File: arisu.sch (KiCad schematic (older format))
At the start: 40 parts, among them J1 USB_B_Micro, J10 PF6, J11 PF7, J12 VCC, J13 D+, J14 D-, J15 GND, J2 MISO, J3 VCC, J4 SCK, J5 MOSI, J6 RES, J7 GND, J8 PF4, J9 PF5, U1 USBLC6-2SC6, U2 ATmega32U4-AU, Y1 Crystal_GND24

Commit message: Initial project update
- Imported FateParts library
- Updated schematic with full backspace switch and stepped capslock switch
- Added new switch footprints to layout
- Updated some traces in layout
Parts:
- U1: symbol Power_Protection:USBLC6-2SC6 -> arisu-rescue:USBLC6-2SC6-Power_Protection
- U2: symbol MCU_Microchip_ATmega:ATmega32U4-AU -> arisu-rescue:ATmega32U4-AU-MCU_Microchip_ATmega
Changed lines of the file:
@@
 EESchema Schematic File Version 4
-LIBS:arisu-cache
-EELAYER 26 0
+EELAYER 30 0
 EELAYER END
 $Descr A4 11693 8268
@@
 $EndDescr
 $Comp
-L MCU_Microchip_ATmega:ATmega32U4-AU U2
+L arisu-rescue:ATmega32U4-AU-MCU_Microchip_ATmega U2
 U 1 1 5C4B1F82
 P 4500 4250
@@
 $EndComp
 $Comp
-L Power_Protection:USBLC6-2SC6 U1
+L arisu-rescue:USBLC6-2SC6-Power_Protection U1
 U 1 1 5C4B2347
 P 1900 5650
@@
 	1    0    0    -1
 $EndComp
+$Comp
+L Mechanical:MountingHole H3
+U 1 1 5C59C18D
+P 8700 3100
+F 0 "H3" H 8800 3146 50  0000 L CNN
+F 1 "MountingHole" H 8800 3055 50  0000 L CNN
+F 2 "Mounting_Holes:MountingHole_2.2mm_M2_Pad" H 8700 3100 50  0001 C CNN
+F 3 "~" H 8700 3100 50  0001 C CNN
+	1    8700 3100
+	1    0    0    -1
+$EndComp
+$Comp
+L Mechanical:MountingHole H4
+U 1 1 5C59C1E9
+P 8700 3300
+F 0 "H4" H 8800 3346 50  0000 L CNN
+F 1 "MountingHole" H 8800 3255 50  0000 L CNN
+F 2 "Mounting_Holes:MountingHole_2.2mm_M2_Pad" H 8700 3300 50  0001 C CNN
+F 3 "~" H 8700 3300 50  0001 C CNN
+	1    8700 3300
+	1    0    0    -1
+$EndComp
+$Comp
+L Mechanical:MountingHole H5
+U 1 1 5C59C249
+P 8700 3500
+F 0 "H5" H 8800 3546 50  0000 L CNN
+F 1 "MountingHole" H 8800 3455 50  0000 L CNN
+F 2 "Mounting_Holes:MountingHole_2.2mm_M2_Pad" H 8700 3500 50  0001 C CNN
+F 3 "~" H 8700 3500 50  0001 C CNN
+	1    8700 3500
+	1    0    0    -1
+$EndComp
+$Comp
+L Mechanical:MountingHole H6
+U 1 1 5C59C2A7
+P 8700 3700
+F 0 "H6" H 8800 3746 50  0000 L CNN
+F 1 "MountingHole" H 8800 3655 50  0000 L CNN
+F 2 "Mounting_Holes:MountingHole_2.2mm_M2_Pad" H 8700 3700 50  0001 C CNN
+F 3 "~" H 8700 3700 50  0001 C CNN
+	1    8700 3700
+	1    0    0    -1
+$EndComp
+$Comp
+L Mechanical:MountingHole H7
+U 1 1 5C59C305
+P 8700 3900
+F 0 "H7" H 8800 3946 50  0000 L CNN
+F 1 "MountingHole" H 8800 3855 50  0000 L CNN
+F 2 "Mounting_Holes:MountingHole_2.2mm_M2_Pad" H 8700 3900 50  0001 C CNN
+F 3 "~" H 8700 3900 50  0001 C CNN
+	1    8700 3900
+	1    0    0    -1
+$EndComp
+$Comp
+L Mechanical:MountingHole H8
+U 1 1 5C59C367
+P 8700 4100
+F 0 "H8" H 8800 4146 50  0000 L CNN
+F 1 "MountingHole" H 8800 4055 50  0000 L CNN
+F 2 "Mounting_Holes:MountingHole_2.2mm_M2_Pad" H 8700 4100 50  0001 C CNN
+F 3 "~" H 8700 4100 50  0001 C CNN
+	1    8700 4100
+	1    0    0    -1
+$EndComp
 Wire Bus Line
 	5750 2700 5750 3150
@@
 Wire Bus Line
 	7050 2650 7050 5800
-$Comp
-L Mechanical:MountingHole H3
-U 1 1 5C59C18D
-P 8700 3100
-F 0 "H3" H 8800 3146 50  0000 L CNN
-F 1 "MountingHole" H 8800 3055 50  0000 L CNN
-F 2 "Mounting_Holes:MountingHole_2.2mm_M2_Pad" H 8700 3100 50  0001 C CNN
-F 3 "~" H 8700 3100 50  0001 C CNN
-	1    8700 3100
-	1    0    0    -1
-$EndComp
-$Comp
-L Mechanical:MountingHole H4
-U 1 1 5C59C1E9
-P 8700 3300
-F 0 "H4" H 8800 3346 50  0000 L CNN
-F 1 "MountingHole" H 8800 3255 50  0000 L CNN
-F 2 "Mounting_Holes:MountingHole_2.2mm_M2_Pad" H 8700 3300 50  0001 C CNN
-F 3 "~" H 8700 3300 50  0001 C CNN
-	1    8700 3300
-	1    0    0    -1
-$EndComp
-$Comp
-L Mechanical:MountingHole H5
-U 1 1 5C59C249
-P 8700 3500
-F 0 "H5" H 8800 3546 50  0000 L CNN
-F 1 "MountingHole" H 8800 3455 50  0000 L CNN
-F 2 "Mounting_Holes:MountingHole_2.2mm_M2_Pad" H 8700 3500 50  0001 C CNN
-F 3 "~" H 8700 3500 50  0001 C CNN
-	1    8700 3500
-	1    0    0    -1
-$EndComp
-$Comp
-L Mechanical:MountingHole H6
-U 1 1 5C59C2A7
-P 8700 3700
-F 0 "H6" H 8800 3746 50  0000 L CNN
-F 1 "MountingHole" H 8800 3655 50  0000 L CNN
-F 2 "Mounting_Holes:MountingHole_2.2mm_M2_Pad" H 8700 3700 50  0001 C CNN
-F 3 "~" H 8700 3700 50  0001 C CNN
-	1    8700 3700
-	1    0    0    -1
-$EndComp
-$Comp
-L Mechanical:MountingHole H7
-U 1 1 5C59C305
-P 8700 3900
-F 0 "H7" H 8800 3946 50  0000 L CNN
-F 1 "MountingHole" H 8800 3855 50  0000 L CNN
-F 2 "Mounting_Holes:MountingHole_2.2mm_M2_Pad" H 8700 3900 50  0001 C CNN
-F 3 "~" H 8700 3900 50  0001 C CNN
-	1    8700 3900
-	1    0    0    -1
-$EndComp
-$Comp
-L Mechanical:MountingHole H8
-U 1 1 5C59C367
-P 8700 4100
-F 0 "H8" H 8800 4146 50  0000 L CNN
-F 1 "MountingHole" H 8800 4055 50  0000 L CNN
-F 2 "Mounting_Holes:MountingHole_2.2mm_M2_Pad" H 8700 4100 50  0001 C CNN
-F 3 "~" H 8700 4100 50  0001 C CNN
-	1    8700 4100
-	1    0    0    -1
-$EndComp
 $EndSCHEMATC

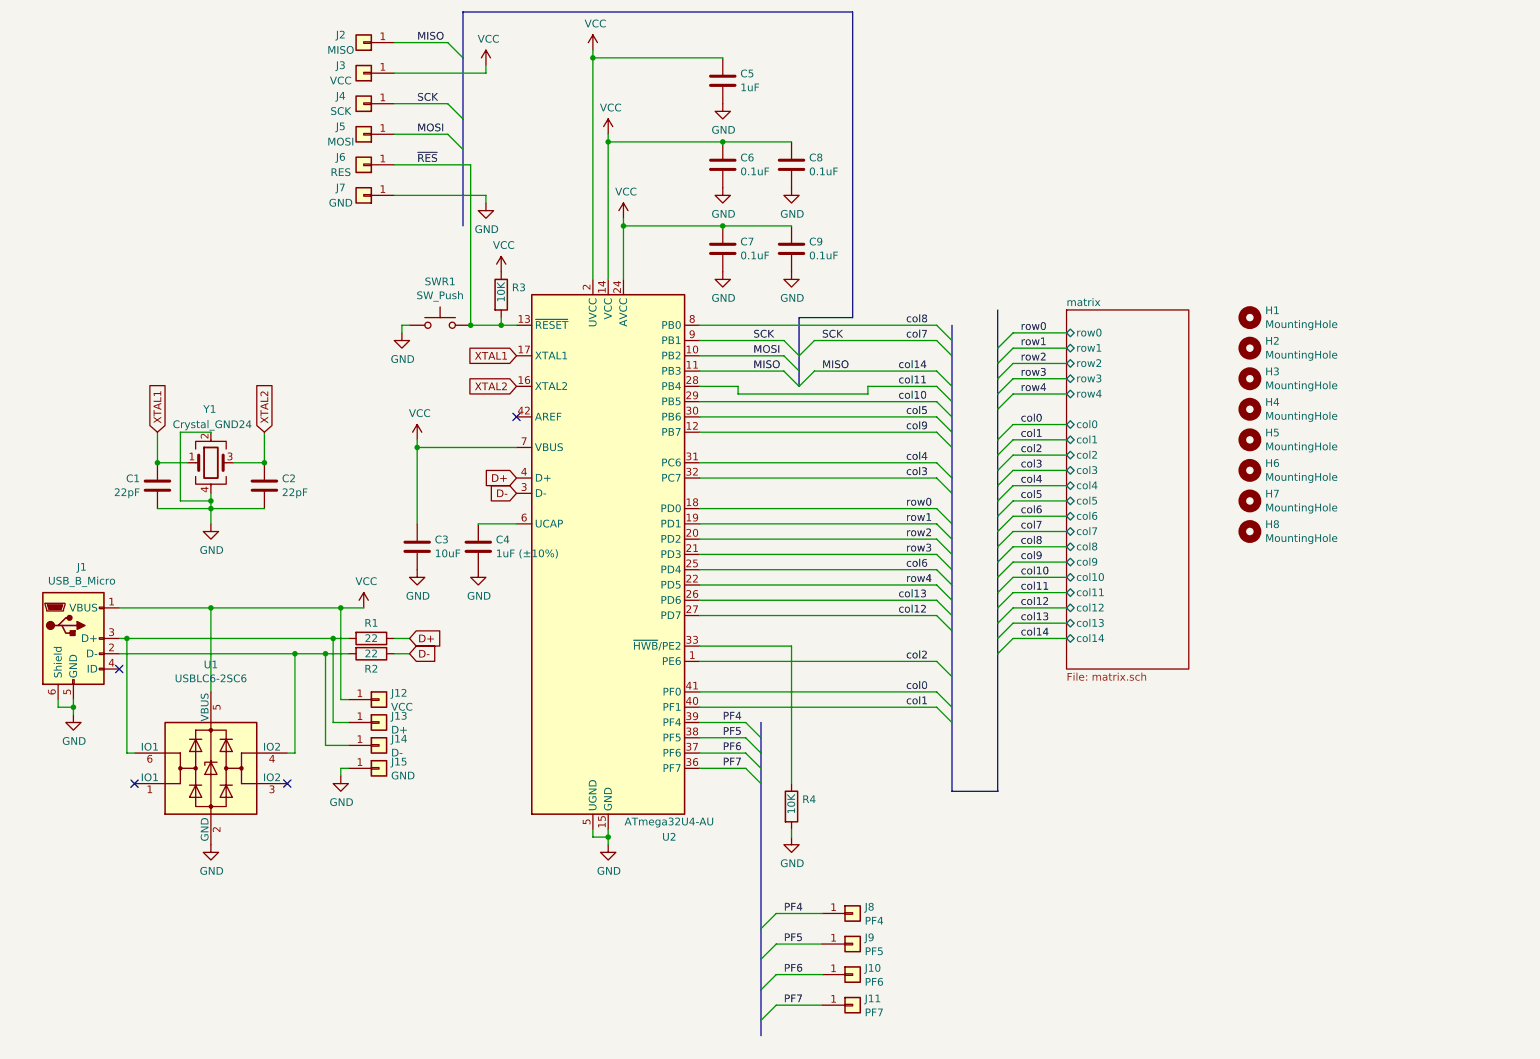
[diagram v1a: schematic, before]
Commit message: Changed mini-USB to USB-C
- Removed mini-USB from schematic and layout
- Added USB-C to schematic and layout
- Added 5k1 resistors for CC1 and CC2 pins, added to layout
- Added bump-out on PCB for USB-C connector to protrude slightly
- Rerouted traces as necessary
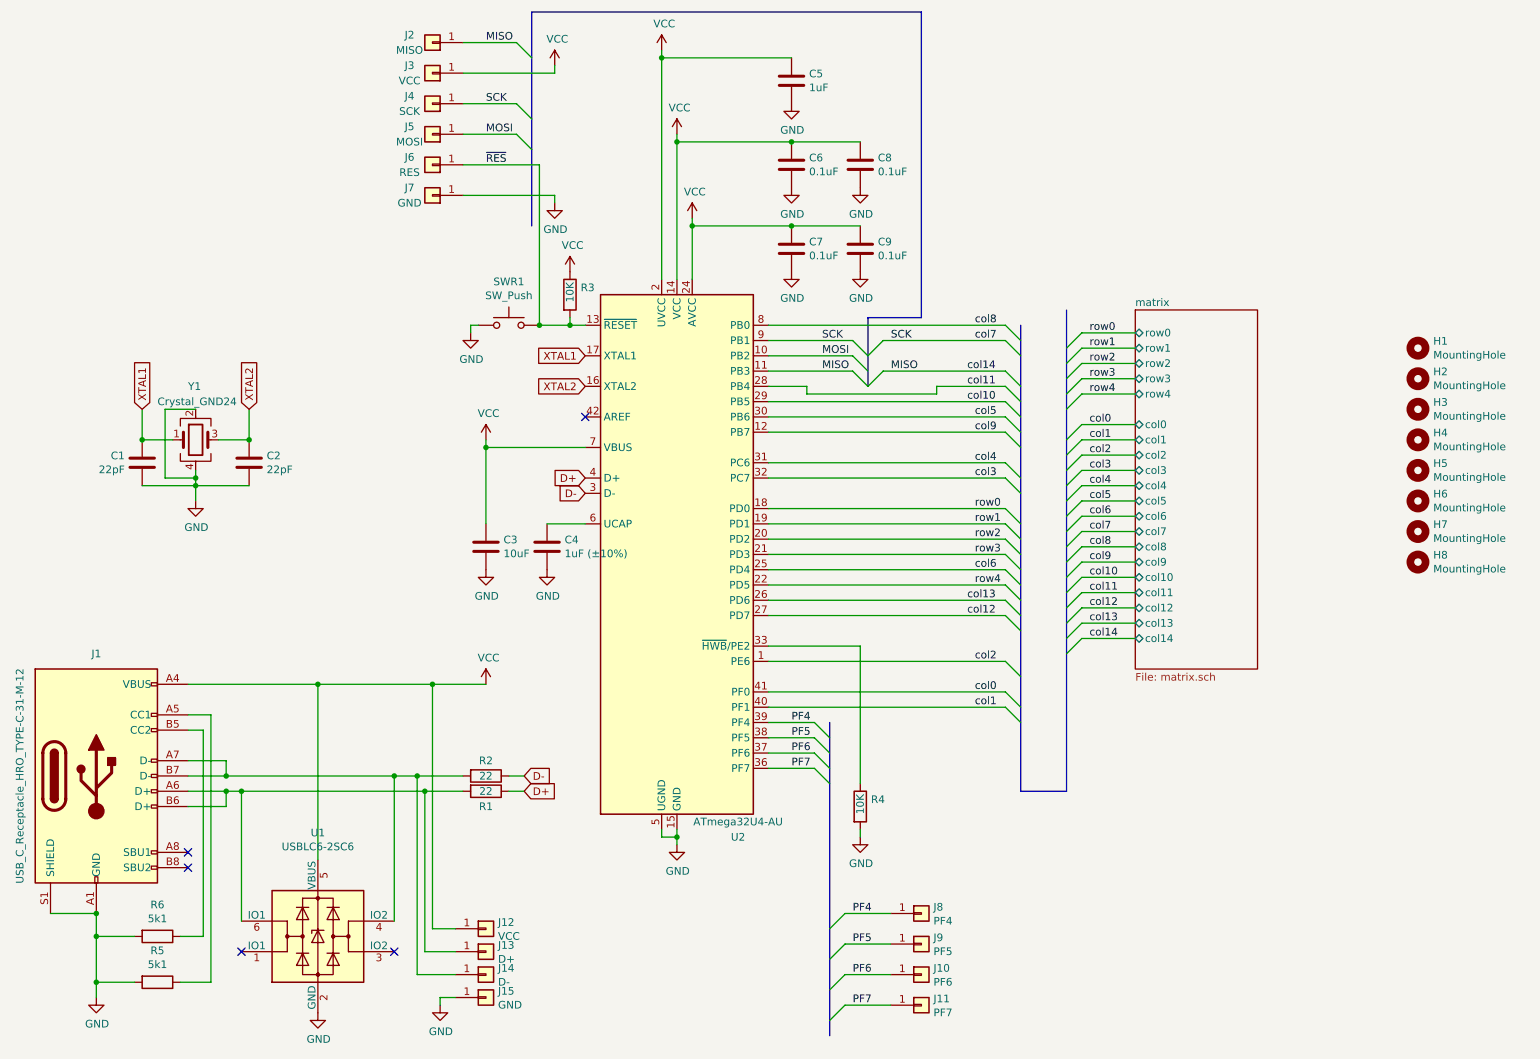
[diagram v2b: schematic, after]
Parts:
- removed J1: USB_B_Micro, Connectors_USB:USB_Micro-B_Molex-105017-0001, symbol Connector:USB_B_Micro
- added J1: USB_C_Receptacle_HRO_TYPE-C-31-M-12, FateParts-USBC:USB_C_Receptacle_HRO_TYPE-C-31-M-12, symbol FateParts-USBC:USB_C_Receptacle_HRO_TYPE-C-31-M-12
- added R5, R6: 5k1, Resistor_SMD:R_0805_2012Metric_Pad1.15x1.40mm_HandSolder, symbol Device:R
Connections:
- net GND: now also J1.A1 (GND), J1.A12 (GND), J1.S1 (SHIELD), R5.2, R6.2
- net VCC: now also J1.A4 (VBUS), J1.A9 (VBUS)
- net at J14.1 (Pin_1), R2.2, U1.4 (IO2): now also J1.A7 (D-), J1.B7 (D-)
- net at J13.1 (Pin_1), R1.2, U1.6 (IO1): now also J1.A6 (D+), J1.B6 (D+)
- new net: J1.A5 (CC1), R5.1
- new net: J1.B5 (CC2), R6.1
- no-connect marks 4 -> 5
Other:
- moved on the sheet: C1, C2, C3, C4, C5, C6, C7, C8, C9, H1, H2, H3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

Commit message: Addition of BOM and position files
- Added JLCPCB part numbers in BOM and exported
- Exported component positioning file
- Some minor cleanup of traces and silkscreen legend positions.
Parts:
- C1, C2: LCSC (none) -> C1804
- C3: LCSC (none) -> C15850
- C4, C5: LCSC (none) -> C28323
- C6, C7, C8, C9: LCSC (none) -> C28233
- R1, R2: LCSC (none) -> C17561
- R3, R4: LCSC (none) -> C17414
- R5, R6: LCSC (none) -> C27834
- SWR1: LCSC (none) -> C318884
- U1: LCSC (none) -> C7519
- U2: LCSC (none) -> C44854
- USB1: renamed from J1; footprint FateParts-USBC:USB_C_Receptacle_HRO_TYPE-C-31-M-12 -> USB_Type-C:USB_C_Receptacle_HRO_TYPE-C-31-M-12; symbol FateParts-USBC:USB_C_Receptacle_HRO_TYPE-C-31-M-12 -> USB_Type-C:USB_C_Receptacle_HRO_TYPE-C-31-M-12
- Y1: LCSC (none) -> C89371
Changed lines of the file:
@@
 F 2 "Housings_QFP:TQFP-44_10x10mm_Pitch0.8mm" H 4950 4250 50  0001 C CIN
 F 3 "http://ww1.microchip.com/downloads/en/DeviceDoc/Atmel-7766-8-bit-AVR-ATmega16U4-32U4_Datasheet.pdf" H 4950 4250 50  0001 C CNN
+F 4 "C44854" H 4950 4250 50  0001 C CNN "LCSC"
 	1    4950 4250
 	1    0    0    -1
@@
 F 2 "TO_SOT_Packages_SMD:SOT-23-6_Handsoldering" H 1850 7150 50  0001 C CNN
 F 3 "http://www2.st.com/resource/en/datasheet/CD00050750.pdf" H 2800 7100 50  0001 C CNN
+F 4 "C7519" H 2600 6750 50  0001 C CNN "LCSC"
 	1    2600 6750
 	1    0    0    -1
@@
 F 2 "Capacitors_SMD:C_0805_HandSoldering" H 4138 4050 50  0001 C CNN
 F 3 "~" H 4100 4200 50  0001 C CNN
+F 4 "C28323" H 4100 4200 50  0001 C CNN "LCSC"
 	1    4100 4200
 	1    0    0    -1
@@
 F 2 "Crystals:Crystal_SMD_SeikoEpson_FA238-4pin_3.2x2.5mm_HandSoldering" H 1800 3500 50  0001 C CNN
 F 3 "~" H 1800 3500 50  0001 C CNN
+F 4 "C89371" H 1800 3500 50  0001 C CNN "LCSC"
 	1    1800 3500
 	1    0    0    -1
@@
 F 2 "Capacitors_SMD:C_0805_HandSoldering" H 1488 3500 50  0001 C CNN
 F 3 "~" H 1450 3650 50  0001 C CNN
+F 4 "C1804" H 1450 3650 50  0001 C CNN "LCSC"
 	1    1450 3650
 	1    0    0    1
@@
 F 2 "Capacitors_SMD:C_0805_HandSoldering" H 2188 3500 50  0001 C CNN
 F 3 "~" H 2150 3650 50  0001 C CNN
+F 4 "C1804" H 2150 3650 50  0001 C CNN "LCSC"
 	1    2150 3650
 	1    0    0    -1
@@
 F 2 "Capacitors_SMD:C_0805_HandSoldering" H 3738 4050 50  0001 C CNN
 F 3 "~" H 3700 4200 50  0001 C CNN
+F 4 "C15850" H 3700 4200 50  0001 C CNN "LCSC"
 	1    3700 4200
 	1    0    0    -1
@@
 F 2 "Buttons_Switches_SMD:SW_SPST_TL3342" H 3850 2950 50  0001 C CNN
 F 3 "" H 3850 2950 50  0001 C CNN
+F 4 "C318884" H 3850 2750 50  0001 C CNN "LCSC"
 	1    3850 2750
 	1    0    0    -1
@@
 F 2 "Resistors_SMD:R_0805_HandSoldering" V 4180 2550 50  0001 C CNN
 F 3 "~" H 4250 2550 50  0001 C CNN
+F 4 "C17414" H 4250 2550 50  0001 C CNN "LCSC"
 	1    4250 2550
 	1    0    0    -1
@@
 F 2 "Capacitors_SMD:C_0805_HandSoldering" H 5738 1000 50  0001 C CNN
 F 3 "~" H 5700 1150 50  0001 C CNN
+F 4 "C28323" H 5700 1150 50  0001 C CNN "LCSC"
 	1    5700 1150
 	1    0    0    -1
@@
 F 2 "Capacitors_SMD:C_0805_HandSoldering" H 5738 1550 50  0001 C CNN
 F 3 "~" H 5700 1700 50  0001 C CNN
+F 4 "C28233" H 5700 1700 50  0001 C CNN "LCSC"
 	1    5700 1700
 	1    0    0    -1
@@
 F 2 "Capacitors_SMD:C_0805_HandSoldering" H 6188 1550 50  0001 C CNN
 F 3 "~" H 6150 1700 50  0001 C CNN
+F 4 "C28233" H 6150 1700 50  0001 C CNN "LCSC"
 	1    6150 1700
 	1    0    0    -1
@@
 F 2 "Capacitors_SMD:C_0805_HandSoldering" H 5738 2100 50  0001 C CNN
 F 3 "~" H 5700 2250 50  0001 C CNN
+F 4 "C28233" H 5700 2250 50  0001 C CNN "LCSC"
 	1    5700 2250
 	1    0    0    -1
@@
 F 2 "Capacitors_SMD:C_0805_HandSoldering" H 6188 2100 50  0001 C CNN
 F 3 "~" H 6150 2250 50  0001 C CNN
+F 4 "C28233" H 6150 2250 50  0001 C CNN "LCSC"
 	1    6150 2250
 	1    0    0    -1
@@
 F 2 "Resistors_SMD:R_0805_HandSoldering" V 6080 5900 50  0001 C CNN
 F 3 "~" H 6150 5900 50  0001 C CNN
+F 4 "C17414" H 6150 5900 50  0001 C CNN "LCSC"
 	1    6150 5900
 	1    0    0    -1
@@
 $EndComp
 $Comp
-L FateParts-USBC:USB_C_Receptacle_HRO_TYPE-C-31-M-12 J1
+L USB_Type-C:USB_C_Receptacle_HRO_TYPE-C-31-M-12 USB1
 U 1 1 5F9245A8
 P 1150 5700
-F 0 "J1" H 1150 6500 50  0000 C CNN
+F 0 "USB1" H 1150 6500 50  0000 C CNN
 F 1 "USB_C_Receptacle_HRO_TYPE-C-31-M-12" V 650 5700 50  0000 C CNN
-F 2 "FateParts-USBC:USB_C_Receptacle_HRO_TYPE-C-31-M-12" H 1300 5700 50  0001 C CNN
+F 2 "USB_Type-C:USB_C_Receptacle_HRO_TYPE-C-31-M-12" H 1300 5700 50  0001 C CNN
 F 3 "" H 1300 5700 50  0001 C CNN
 	1    1150 5700
@@
 F 2 "Resistor_SMD:R_0805_2012Metric_Pad1.15x1.40mm_HandSolder" V 1480 7050 50  0001 C CNN
 F 3 "~" H 1550 7050 50  0001 C CNN
+F 4 "C27834" H 1550 7050 50  0001 C CNN "LCSC"
 	1    1550 7050
 	0    1    1    0
@@
 F 2 "Resistor_SMD:R_0805_2012Metric_Pad1.15x1.40mm_HandSolder" V 1480 6750 50  0001 C CNN
 F 3 "~" H 1550 6750 50  0001 C CNN
+F 4 "C27834" H 1550 6750 50  0001 C CNN "LCSC"
 	1    1550 6750
 	0    1    1    0
@@
 Wire Wire Line
 	1150 6600 1150 6750
-Connection ~ 1150 6600
 Wire Wire Line
 	1400 7050 1150 7050
@@
 F 2 "Resistors_SMD:R_0805_HandSoldering" V 3630 5700 50  0001 C CNN
 F 3 "~" H 3700 5700 50  0001 C CNN
+F 4 "C17561" H 3700 5700 50  0001 C CNN "LCSC"
 	1    3700 5700
 	0    1    1    0
@@
 F 2 "Resistors_SMD:R_0805_HandSoldering" V 3630 5800 50  0001 C CNN
 F 3 "~" H 3700 5800 50  0001 C CNN
+F 4 "C17561" H 3700 5800 50  0001 C CNN "LCSC"
 	1    3700 5800
 	0    1    1    0

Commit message: Small cleanup and updates
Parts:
- U2: footprint Housings_QFP:TQFP-44_10x10mm_Pitch0.8mm -> Package_QFP:TQFP-44_10x10mm_P0.8mm
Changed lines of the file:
@@
 F 0 "U2" H 5350 2400 50  0000 C CNN
 F 1 "ATmega32U4-AU" H 5350 2500 50  0000 C CNN
-F 2 "Housings_QFP:TQFP-44_10x10mm_Pitch0.8mm" H 4950 4250 50  0001 C CIN
+F 2 "Package_QFP:TQFP-44_10x10mm_P0.8mm" H 4950 4250 50  0001 C CIN
 F 3 "http://ww1.microchip.com/downloads/en/DeviceDoc/Atmel-7766-8-bit-AVR-ATmega16U4-32U4_Datasheet.pdf" H 4950 4250 50  0001 C CNN
 F 4 "C44854" H 4950 4250 50  0001 C CNN "LCSC"
